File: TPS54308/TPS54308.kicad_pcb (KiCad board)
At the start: 2 copper layers, 25.4 x 12.7 mm, 14 parts, among them P1 CONN_01X04, P2 CONN_01X04, U1 TPS54308DDC

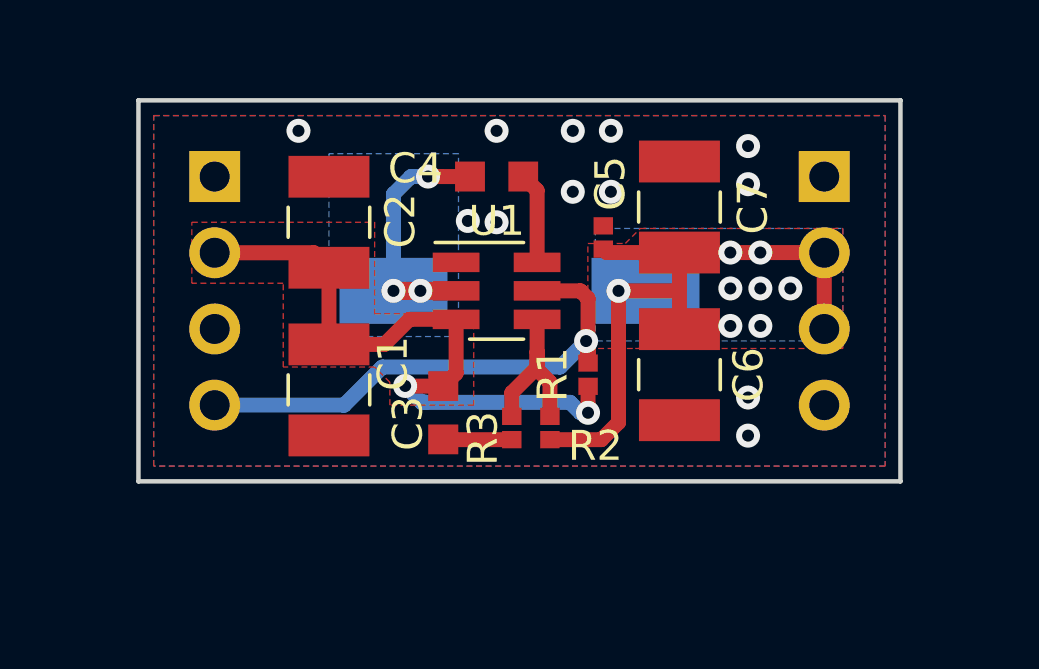
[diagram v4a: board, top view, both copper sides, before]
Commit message: moved parts of silkscreen
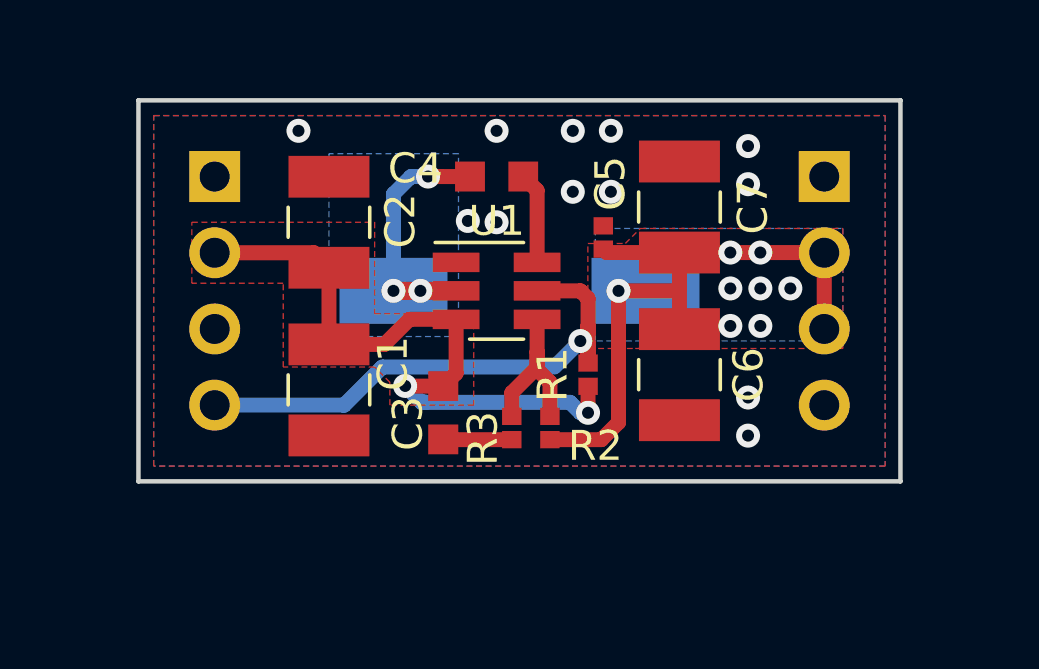
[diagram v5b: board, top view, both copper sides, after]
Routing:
- net EN: track 18.1 -> 19.1 mm
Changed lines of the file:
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@@
-(kicad_pcb (version 20171130) (host pcbnew "(5.0.0-rc3-dev)")
+(kicad_pcb (version 20171130) (host pcbnew "(5.0.0)")
   (general
     (thickness 1.6)
     (drawings 6)
-    (tracks 91)
+    (tracks 94)
     (zones 0)
     (modules 14)
@@
       (psa4output false)
       (plotreference true)
-      (plotvalue true)
+      (plotvalue false)
       (plotinvisibletext false)
       (padsonsilk false)
@@
       (outputformat 1)
       (mirror false)
-      (drillshape 1)
+      (drillshape 0)
       (scaleselection 1)
       (outputdirectory ""))
@@
   (segment (start 111.252 100.33) (end 109.808 100.33) (width 0.5) (layer F.Cu) (net 4))
   (segment (start 111.506 100.584) (end 111.252 100.33) (width 0.5) (layer F.Cu) (net 4))
-  (segment (start 111.506 102.7365) (end 111.506 100.584) (width 0.5) (layer F.Cu) (net 4))
-  (via (at 111.441759 102.002915) (size 0.8) (drill 0.4) (layers F.Cu B.Cu) (net 4))
-  (segment (start 111.479999 101.964675) (end 111.441759 102.002915) (width 0.5) (layer B.Cu) (net 4))
-  (segment (start 111.479999 101.880001) (end 111.479999 101.964675) (width 0.5) (layer B.Cu) (net 4))
+  (via (at 111.25 102.002915) (size 0.8) (drill 0.4) (layers F.Cu B.Cu) (net 4))
   (segment (start 111.506 102.067156) (end 111.441759 102.002915) (width 0.5) (layer F.Cu) (net 4))
   (segment (start 111.506 102.7365) (end 111.506 102.067156) (width 0.5) (layer F.Cu) (net 4))
-  (segment (start 110.574674 102.87) (end 111.441759 102.002915) (width 0.5) (layer B.Cu) (net 4))
-  (segment (start 104.648 102.87) (end 110.574674 102.87) (width 0.5) (layer B.Cu) (net 4))
   (segment (start 99.06 104.14) (end 103.378 104.14) (width 0.5) (layer B.Cu) (net 4))
   (segment (start 103.378 104.14) (end 104.648 102.87) (width 0.5) (layer B.Cu) (net 4))
+  (segment (start 111.25 102.002915) (end 110.382915 102.87) (width 0.5) (layer B.Cu) (net 4))
+  (segment (start 104.648 102.87) (end 110.25 102.87) (width 0.5) (layer B.Cu) (net 4))
+  (segment (start 111.506 101.746915) (end 111.25 102.002915) (width 0.5) (layer F.Cu) (net 4))
+  (segment (start 111.506 101.5) (end 111.506 101.746915) (width 0.5) (layer F.Cu) (net 4))
+  (segment (start 111.506 101.5) (end 111.506 100.584) (width 0.5) (layer F.Cu) (net 4))
+  (segment (start 111.506 102.7365) (end 111.506 101.5) (width 0.5) (layer F.Cu) (net 4))
+  (segment (start 111.506 102.258915) (end 111.25 102.002915) (width 0.5) (layer F.Cu) (net 4))
+  (segment (start 111.506 102.7365) (end 111.506 102.258915) (width 0.5) (layer F.Cu) (net 4))
   (segment (start 109.808 102.885) (end 109.808 102.362) (width 0.5) (layer F.Cu) (net 5))
   (segment (start 108.966 103.727) (end 109.808 102.885) (width 0.5) (layer F.Cu) (net 5))

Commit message: new pinout
changed to a sideway standing pinout and rearranged components accordingly
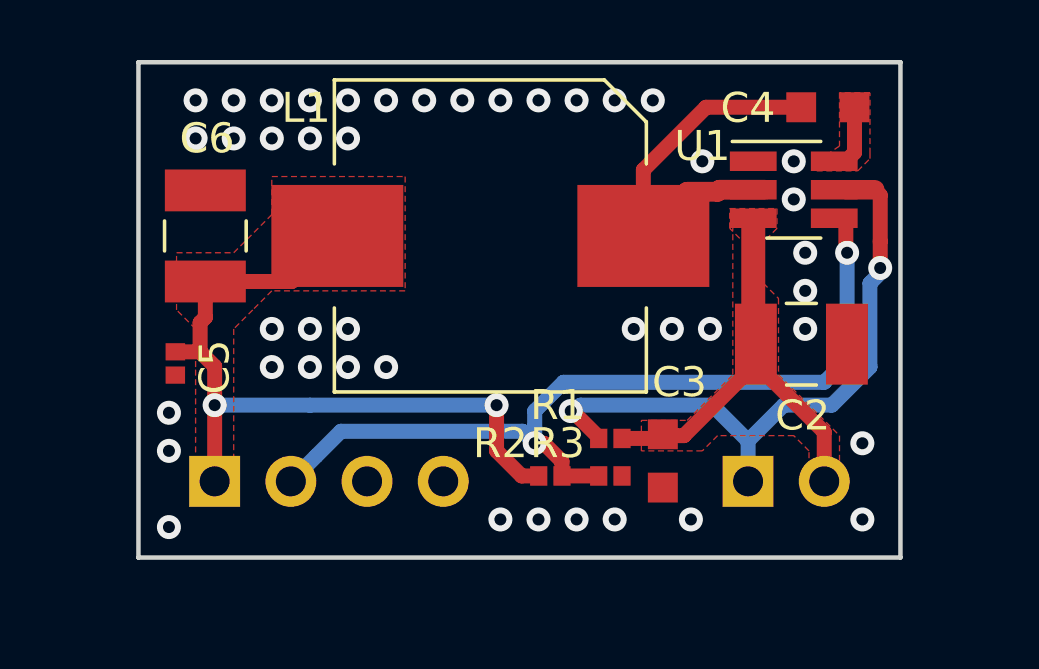
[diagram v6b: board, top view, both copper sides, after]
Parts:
- removed C1: 10u/50V/1210, Capacitor_SMD:C_1210_3225Metric_Pad1.39x2.70mm_HandSolder
- removed C7: 22u/6.3V/1210, Capacitor_SMD:C_1210_3225Metric_Pad1.39x2.70mm_HandSolder
- L1: value L -> 7447798131_13uH_5.85A; footprint Inductor_SMD:L_Wuerth_WE-PD-Typ-M-Typ-S_Handsoldering -> Inductor_SMD:L_Wuerth_WE-PDF_Handsoldering; moved to F.Cu
- P1: value CONN_01X04 -> CONN_01X02; footprint Connector_PinHeader_2.54mm:PinHeader_1x04_P2.54mm_Vertical -> Connector_PinHeader_2.54mm:PinHeader_1x02_P2.54mm_Horizontal
- P2: footprint Connector_PinHeader_2.54mm:PinHeader_1x04_P2.54mm_Vertical -> Connector_PinHeader_2.54mm:PinHeader_1x04_P2.54mm_Horizontal
- moved P2 22.7 mm to (99.1, 106.7), turned to 270 degrees
- moved P1 20.5 mm to (116.8, 106.7), turned to 270 degrees
- moved C6 16.5 mm to (98.8, 98.5), turned to 90 degrees
- moved C2 16.3 mm to (118.6, 102.1), turned to 0 degrees
- moved C5 14.9 mm to (97.8, 102.8), turned to 270 degrees
- moved C4 11.3 mm to (119.5, 94.2)
- moved U1 10.5 mm to (118.4, 97.0)
- moved C3 7.49 mm to (114.0, 106.0)
- moved R3 3.65 mm to (112.2, 106.5), turned to 0 degrees
- moved R1 2.25 mm to (112.2, 105.2), turned to 180 degrees
- moved L1 2.07 mm to (108.2, 98.5), turned to 180 degrees
- moved R2 1.60 mm to (110.2, 106.5), turned to 0 degrees
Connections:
- P1 pad 1: GND -> EN
- P2 pad 1: GND -> VOUT
- P2 pad 2: VOUT -> FB
- P2 pad 3: VOUT -> GND
- P2 pad 4: GND -> Net-(P2-Pad4)
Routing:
- net FB: track 5.91 -> 28.8 mm, vias 0 -> 2
- net VIN: track 22.5 -> 15.6 mm, vias 2 -> 0
- net SW: track 7.97 -> 13.5 mm, vias 3 -> 0
- net VOUT: track 22.7 -> 25.5 mm, vias 8 -> 2
- net GND: track 2.29 -> 0.00 mm, vias 12 -> 44
- net EN: track 19.1 -> 21.3 mm, vias 1 -> 2
- net BOOT: track 3.05 -> 1.92 mm
- added copper zone on F.Cu, net BOOT
- removed copper zone on B.Cu, net SW
- removed copper zone on B.Cu, net VOUT
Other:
- board size 25.4 x 12.7 mm -> 25.4 x 16.5 mm

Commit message: Ready for first test run
Changed back to more compact coil
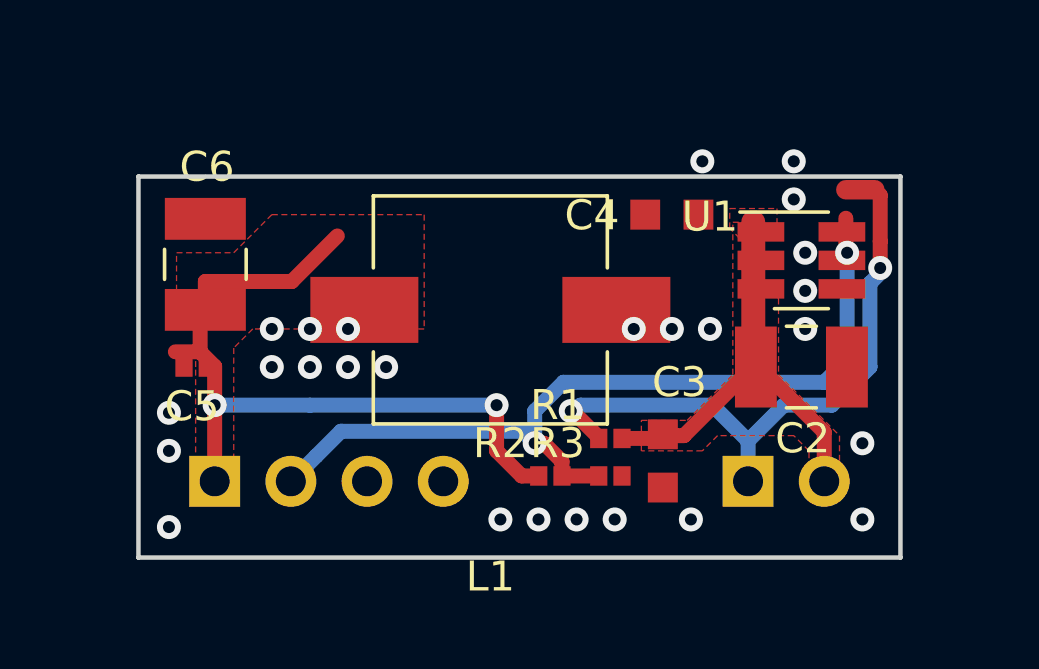
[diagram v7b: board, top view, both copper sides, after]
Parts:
- L1: value 7447798131_13uH_5.85A -> 74437346082_8u2_3.25A; footprint Inductor_SMD:L_Wuerth_WE-PDF_Handsoldering -> Inductor_SMD:L_Wuerth_WE-PD-Typ-M-Typ-S_Handsoldering
- moved C4 6.31 mm to (114.3, 97.8)
- moved L1 2.47 mm to (108.2, 101.0)
- moved U1 2.37 mm to (118.6, 99.3)
- moved C6 0.95 mm to (98.8, 99.4)
- moved C2 0.76 mm to (118.6, 102.9)
- moved C5 0.69 mm to (98.4, 102.9), turned to 180 degrees
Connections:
- L1 pad 1: SW -> Net-(L1-Pad1)
- L1 pad 2: VOUT -> Net-(L1-Pad2)
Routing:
- net SW: track 13.5 -> 0.00 mm, vias 0 -> 1
- net BOOT: track 1.92 -> 0.00 mm
- net Net-(L1-Pad2): vias 0 -> 1
- net Net-(L1-Pad1): vias 0 -> 1
- net GND: vias 44 -> 23
- removed copper zone on F.Cu, net BOOT
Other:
- board size 25.4 x 16.5 mm -> 25.4 x 12.7 mm

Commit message: finished routing
...but not yet satisfied as the gnd path between input and output capacitor is way too long.
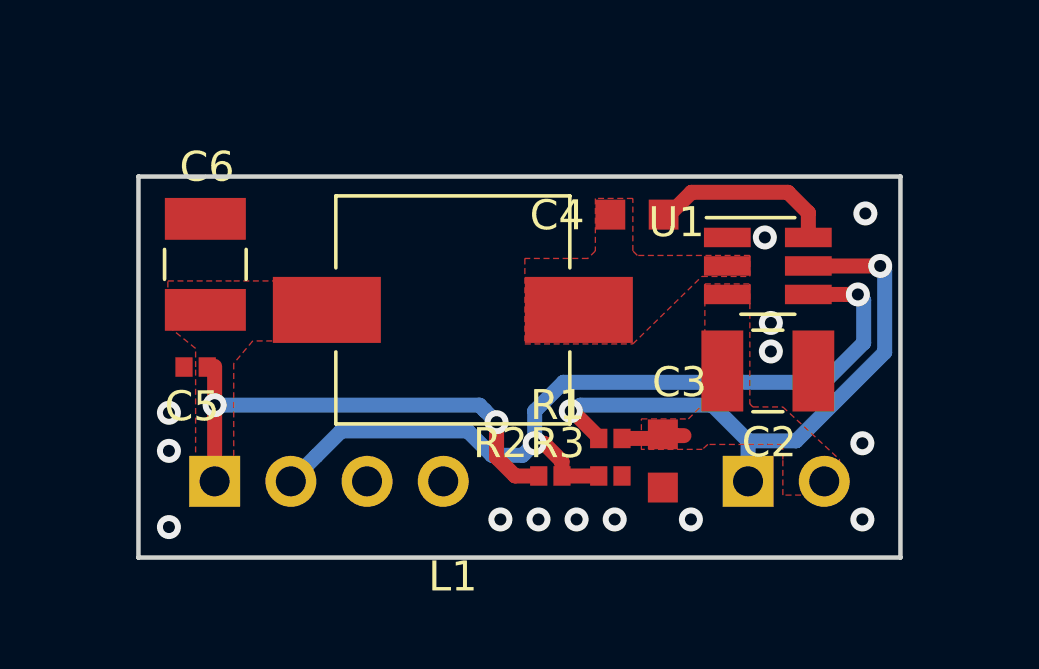
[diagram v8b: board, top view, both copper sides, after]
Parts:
- moved L1 1.25 mm to (107.0, 101.0)
- moved C4 1.16 mm to (113.1, 97.8)
- moved U1 1.13 mm to (117.5, 99.5)
- moved C2 1.13 mm to (117.5, 103.0)
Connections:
- L1 pad 1: Net-(L1-Pad1) -> SW
- L1 pad 2: Net-(L1-Pad2) -> VOUT
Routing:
- net VIN: track 15.6 -> 2.49 mm
- net VOUT: track 25.5 -> 16.5 mm
- net BOOT: track 0.00 -> 6.24 mm
- net EN: track 21.3 -> 20.3 mm
- net SW: vias 1 -> 0
- net Net-(L1-Pad2): vias 1 -> 0
- net Net-(L1-Pad1): vias 1 -> 0
- net GND: vias 23 -> 14
- added copper zone on F.Cu, net SW
